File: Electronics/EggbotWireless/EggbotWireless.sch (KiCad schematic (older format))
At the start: 55 parts, among them J1 BATT, J2 Conn_01x04_Female, J3 USB_B_Micro, J4 AVR-ISP-6, J5 Conn_01x03_Female, M1 Stepper_Motor_bipolar, M2 Stepper_Motor_bipolar, Q1 FDD8447L, U1 TPS62203DBV, U2 ATmega16A-AU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

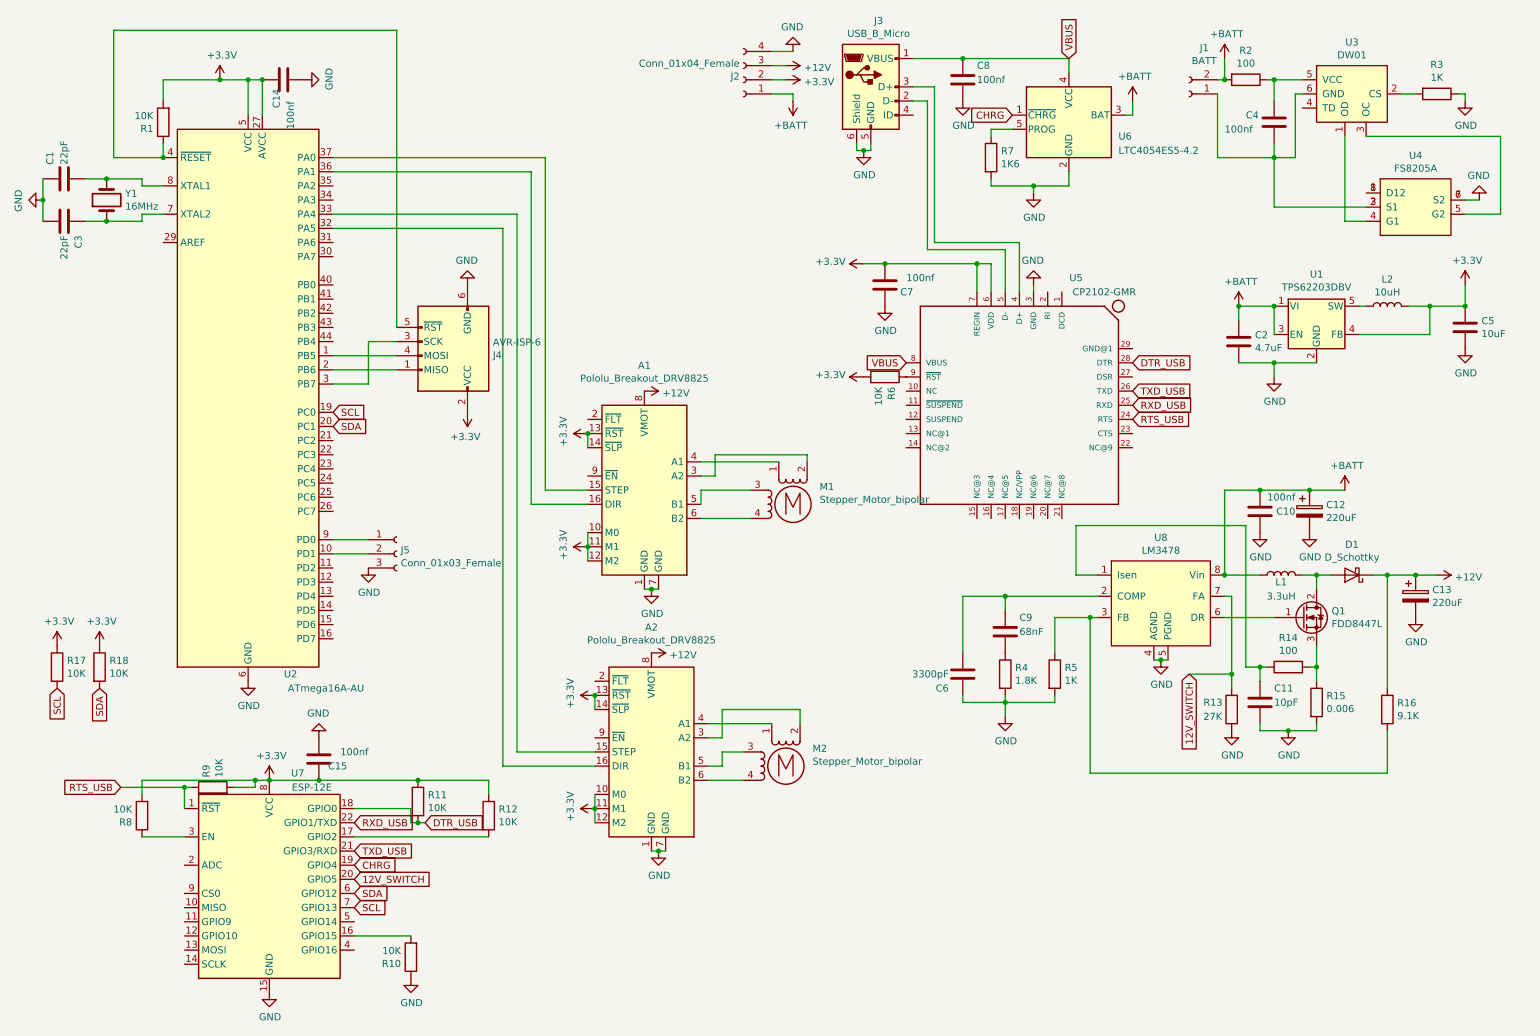
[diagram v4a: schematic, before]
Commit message: add switch to the board
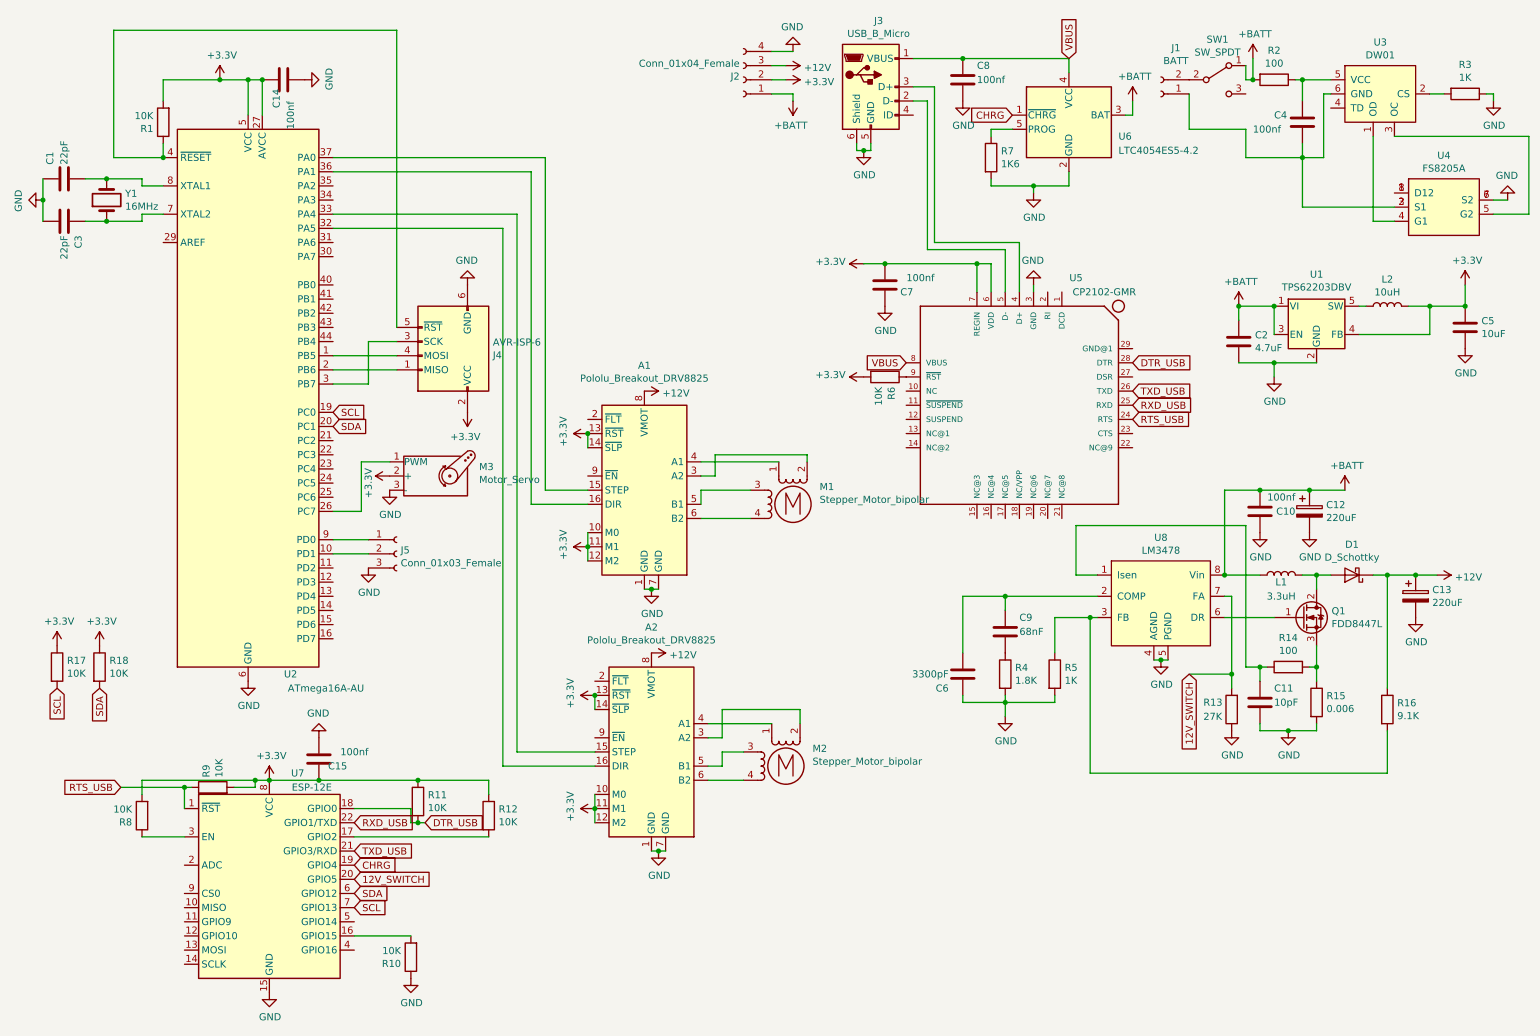
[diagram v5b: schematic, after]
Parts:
- added M3: Motor_Servo, Connector_PinSocket_2.54mm:PinSocket_1x03_P2.54mm_Vertical, symbol Motor:Motor_Servo
- added SW1: SW_SPDT, Button_Switch_THT:SW_CuK_OS102011MA1QN1_SPDT_Angled, symbol Switch:SW_SPDT
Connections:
- net +3V3: now also M3.2 (+)
- net +BATT: now also SW1.1 (A); no longer J1.2 (Pin_2)
- net GND: now also M3.3 (-)
- net at U2.26 (PC7): now also M3.1 (PWM)
- new net: J1.2 (Pin_2), SW1.2 (B)
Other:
- moved on the sheet: C4, J1, R2, R3, U3, U4

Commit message: change atmega16 to atmega32 in schematic
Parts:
- U2: value ATmega16A-AU -> ATmega32A-AU; symbol MCU_Microchip_ATmega:ATmega16A-AU -> MCU_Microchip_ATmega:ATmega32A-AU
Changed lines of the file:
@@
 Connection ~ 1550 1500
 $Comp
-L MCU_Microchip_ATmega:ATmega16A-AU U2
+L MCU_Microchip_ATmega:ATmega32A-AU U2
 U 1 1 5CE9956C
 P 2150 3200
 F 0 "U2" H 2450 1250 50  0000 C CNN
-F 1 "ATmega16A-AU" H 2700 1150 50  0000 C CNN
+F 1 "ATmega32A-AU" H 2700 1150 50  0000 C CNN
 F 2 "Package_QFP:TQFP-44_10x10mm_P0.8mm" H 2150 3200 50  0001 C CIN
 F 3 "http://ww1.microchip.com/downloads/en/DeviceDoc/Atmel-8154-8-bit-AVR-ATmega16A_Datasheet.pdf" H 2150 3200 50  0001 C CNN

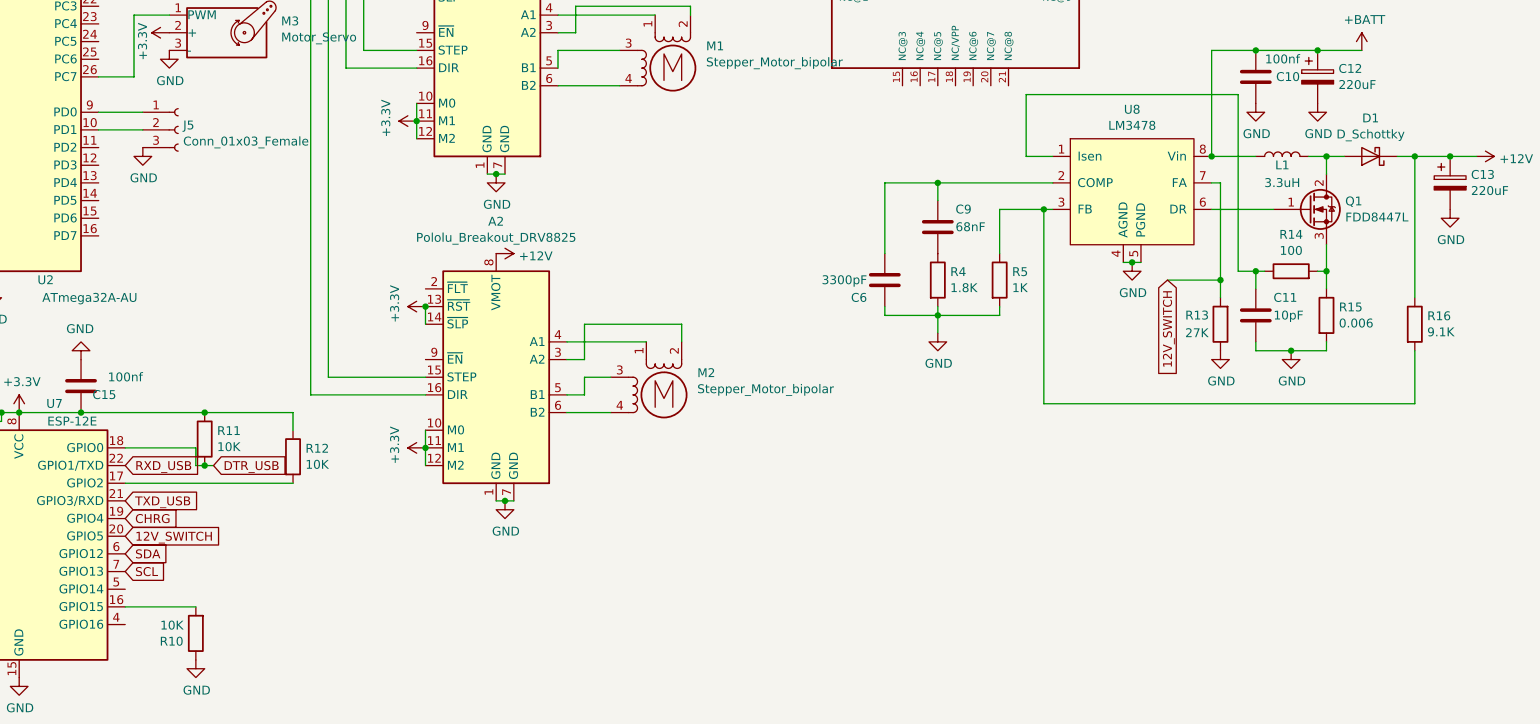
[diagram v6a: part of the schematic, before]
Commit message: proper 12v shutdown circuit
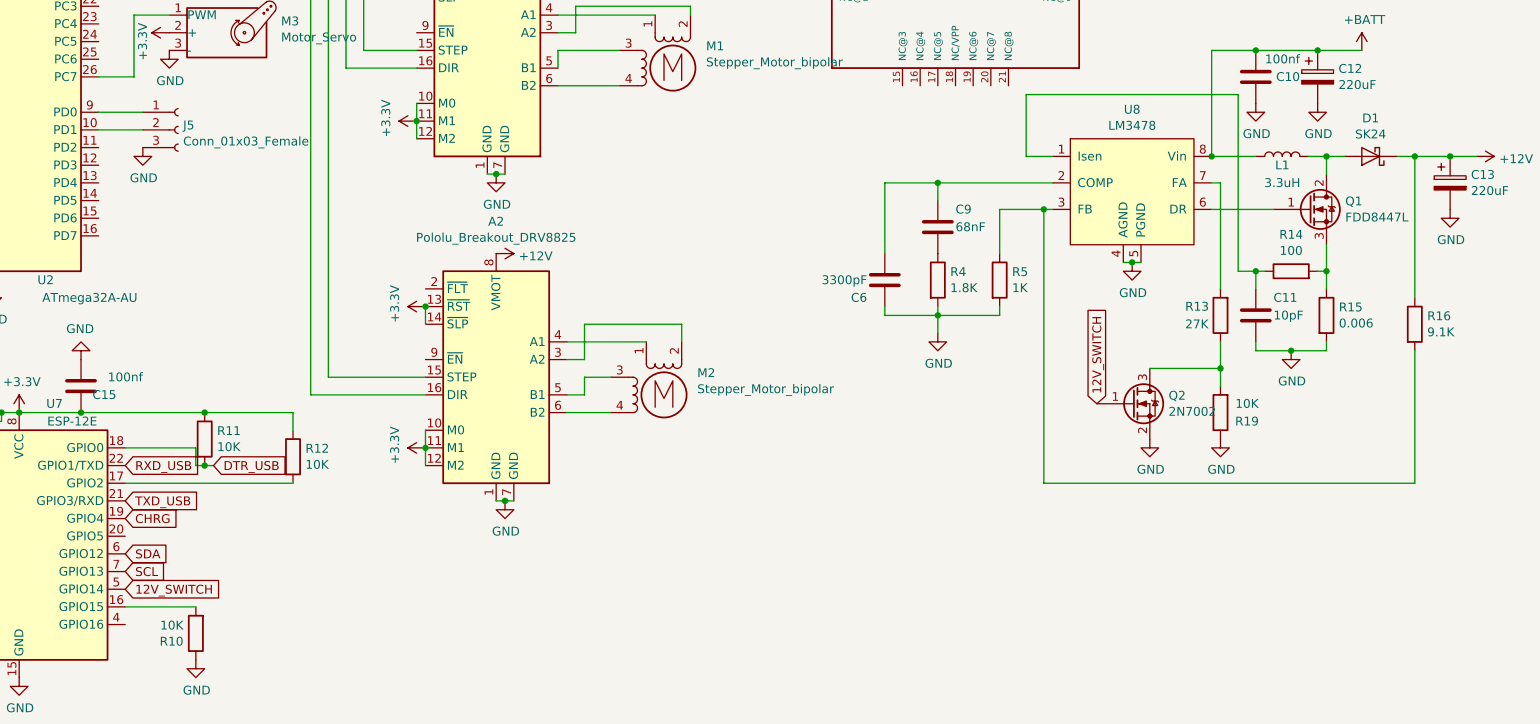
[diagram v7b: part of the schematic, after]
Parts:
- added Q2: 2N7002, Package_TO_SOT_SMD:SOT-23, symbol Transistor_FET:2N7002
- added R19: 10K, Resistor_SMD:R_0805_2012Metric_Pad1.15x1.40mm_HandSolder, symbol Device:R
- D1: value D_Schottky -> SK24; footprint Diode_SMD:D_SMA_Handsoldering -> Diode_SMD:D_SMB_Handsoldering
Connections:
- net 12V_SWITCH: now also U7.5 (GPIO14), Q2.1 (G); no longer R13.2, U7.20 (GPIO5), U8.7 (FA)
- net GND: now also Q2.2 (S), R19.1; no longer R13.1
- new net: R13.2, U8.7 (FA)
- new net: Q2.3 (D), R13.1, R19.2
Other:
- moved on the sheet: R13
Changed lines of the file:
@@
 P 9950 4450
 F 0 "D1" H 9950 4234 50  0000 C CNN
-F 1 "D_Schottky" H 9950 4325 50  0000 C CNN
-F 2 "Diode_SMD:D_SMA_Handsoldering" H 9950 4450 50  0001 C CNN
+F 1 "SK24" H 9950 4325 50  0000 C CNN
+F 2 "Diode_SMD:D_SMB_Handsoldering" H 9950 4450 50  0001 C CNN
 F 3 "~" H 9950 4450 50  0001 C CNN
 	1    9950 4450
@@
 	1    0    0    -1
 $EndComp
-Text GLabel 2900 6600 2    50   Input ~ 0
+Text GLabel 2900 6900 2    50   Input ~ 0
 12V_SWITCH
-Text GLabel 8800 5150 3    50   Input ~ 0
+Text GLabel 8400 5850 1    50   Input ~ 0
 12V_SWITCH
 $Comp
@@
 	10200 4450 10400 4450
 Wire Wire Line
-	10200 5550 10200 5850
-Wire Wire Line
-	8100 5850 8100 4750
+	10200 5550 10200 6300
+Wire Wire Line
+	8100 6300 8100 4750
 Wire Wire Line
 	8150 4750 8100 4750
@@
 Connection ~ 7500 5350
 Wire Wire Line
-	8100 5850 10200 5850
+	8100 6300 10200 6300
 Wire Wire Line
 	7500 4700 7500 4600
@@
 L Device:R R13
 U 1 1 5D0DA168
-P 9100 5400
-F 0 "R13" H 9300 5350 50  0000 R CNN
-F 1 "27K" H 9300 5450 50  0000 R CNN
-F 2 "Resistor_SMD:R_0805_2012Metric_Pad1.15x1.40mm_HandSolder" V 9030 5400 50  0001 C CNN
-F 3 "~" H 9100 5400 50  0001 C CNN
-	1    9100 5400
+P 9100 5350
+F 0 "R13" H 9300 5300 50  0000 R CNN
+F 1 "27K" H 9300 5400 50  0000 R CNN
+F 2 "Resistor_SMD:R_0805_2012Metric_Pad1.15x1.40mm_HandSolder" V 9030 5350 50  0001 C CNN
+F 3 "~" H 9100 5350 50  0001 C CNN
+	1    9100 5350
 	-1   0    0    1
-$EndComp
-$Comp
-L EggbotWireless-rescue:GND-power-Catfi-rescue #PWR0135
-U 1 1 5D0DAD88
-P 9100 5550
-F 0 "#PWR0135" H 9100 5300 50  0001 C CNN
-F 1 "GND" H 9105 5377 50  0000 C CNN
-F 2 "" H 9100 5550 50  0001 C CNN
-F 3 "" H 9100 5550 50  0001 C CNN
-	1    9100 5550
-	1    0    0    -1
 $EndComp
 Wire Wire Line
@@
 	0    -1   -1   0
 $EndComp
-Wire Wire Line
-	8800 5150 9100 5150
-Wire Wire Line
-	9100 4600 9100 5150
-Connection ~ 9100 5150
-Wire Wire Line
-	9100 5150 9100 5250
 $Comp
 L Driver_Motor:Pololu_Breakout_DRV8825 A1
@@
 Wire Wire Line
 	9200 850  9200 950
+$Comp
+L Device:R R19
+U 1 1 5CECA907
+P 9100 5900
+F 0 "R19" H 8950 5950 50  0000 C CNN
+F 1 "10K" H 8950 5850 50  0000 C CNN
+F 2 "Resistor_SMD:R_0805_2012Metric_Pad1.15x1.40mm_HandSolder" V 9030 5900 50  0001 C CNN
+F 3 "~" H 9100 5900 50  0001 C CNN
+	1    9100 5900
+	-1   0    0    1
+$EndComp
+$Comp
+L EggbotWireless-rescue:GND-power-Catfi-rescue #PWR0135
+U 1 1 5D0DAD88
+P 9100 6050
+F 0 "#PWR0135" H 9100 5800 50  0001 C CNN
+F 1 "GND" H 9105 5877 50  0000 C CNN
+F 2 "" H 9100 6050 50  0001 C CNN
+F 3 "" H 9100 6050 50  0001 C CNN
+	1    9100 6050
+	1    0    0    -1
+$EndComp
+Wire Wire Line
+	9100 4600 9100 5200
+$Comp
+L Transistor_FET:2N7002 Q2
+U 1 1 5CF2F5A0
+P 8600 5850
+F 0 "Q2" H 8806 5896 50  0000 L CNN
+F 1 "2N7002" H 8806 5805 50  0000 L CNN
+F 2 "Package_TO_SOT_SMD:SOT-23" H 8800 5775 50  0001 L CIN
+F 3 "https://www.fairchildsemi.com/datasheets/2N/2N7002.pdf" H 8600 5850 50  0001 L CNN
+	1    8600 5850
+	1    0    0    -1
+$EndComp
+Wire Wire Line
+	8700 5650 9100 5650
+Wire Wire Line
+	9100 5500 9100 5650
+Connection ~ 9100 5650
+Wire Wire Line
+	9100 5650 9100 5750
+$Comp
+L EggbotWireless-rescue:GND-power-Catfi-rescue #PWR0152
+U 1 1 5CFAA2C4
+P 8700 6050
+F 0 "#PWR0152" H 8700 5800 50  0001 C CNN
+F 1 "GND" H 8705 5877 50  0000 C CNN
+F 2 "" H 8700 6050 50  0001 C CNN
+F 3 "" H 8700 6050 50  0001 C CNN
+	1    8700 6050
+	1    0    0    -1
+$EndComp
 $EndSCHEMATC

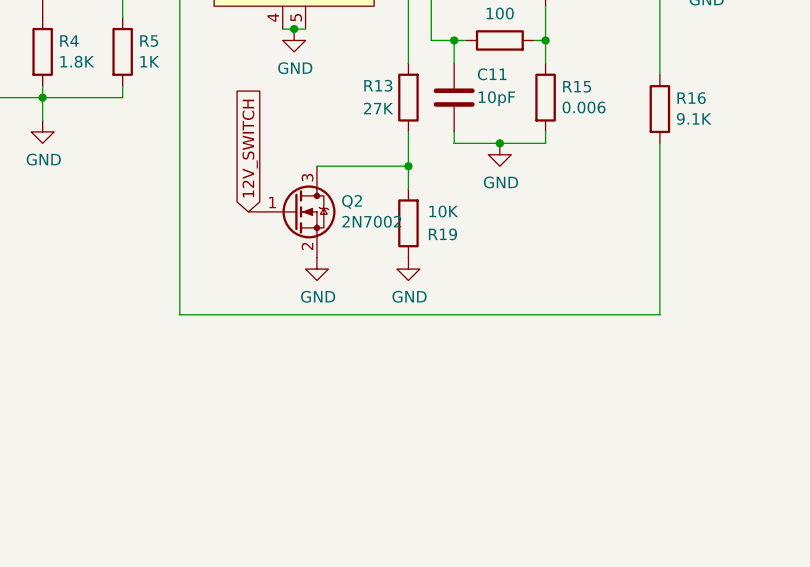
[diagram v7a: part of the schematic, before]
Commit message: fix shutdown circuit
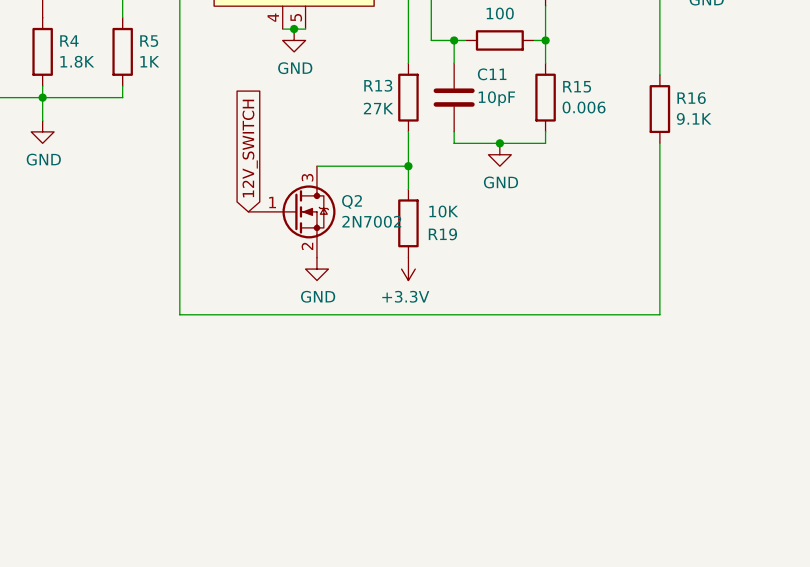
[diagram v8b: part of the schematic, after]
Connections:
- net +3V3: now also R19.1
- net GND: no longer R19.1
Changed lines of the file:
@@
 	-1   0    0    1
-$EndComp
-$Comp
-L EggbotWireless-rescue:GND-power-Catfi-rescue #PWR0135
-U 1 1 5D0DAD88
-P 9100 6050
-F 0 "#PWR0135" H 9100 5800 50  0001 C CNN
-F 1 "GND" H 9105 5877 50  0000 C CNN
-F 2 "" H 9100 6050 50  0001 C CNN
-F 3 "" H 9100 6050 50  0001 C CNN
-	1    9100 6050
-	1    0    0    -1
 $EndComp
 Wire Wire Line
@@
 	1    0    0    -1
 $EndComp
+$Comp
+L power:+3.3V #PWR0135
+U 1 1 5CEC8E18
+P 9100 6050
+F 0 "#PWR0135" H 9100 5900 50  0001 C CNN
+F 1 "+3.3V" H 9115 6223 50  0000 C CNN
+F 2 "" H 9100 6050 50  0001 C CNN
+F 3 "" H 9100 6050 50  0001 C CNN
+	1    9100 6050
+	-1   0    0    1
+$EndComp
 $EndSCHEMATC
